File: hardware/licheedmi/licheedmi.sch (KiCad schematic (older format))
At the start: 70 parts, among them J1 Conn_01x09, J2 HDMI_A_PCB, J3 LicheePiNano_LCD, J4 HDMI_A, J5 USB_C_Receptacle_USB2.0, U1 TDA19988, U2 LicheeNano, U3 TS3DV20812, U4 SC6206B, U5 CH340C

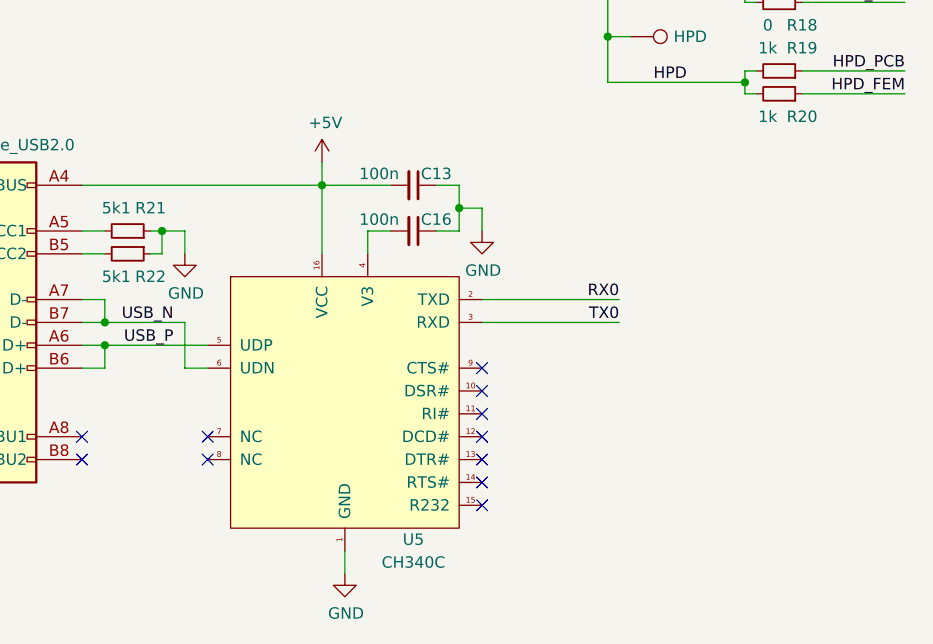
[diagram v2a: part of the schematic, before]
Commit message: sch, pcb: Add UART0 activity LEDs
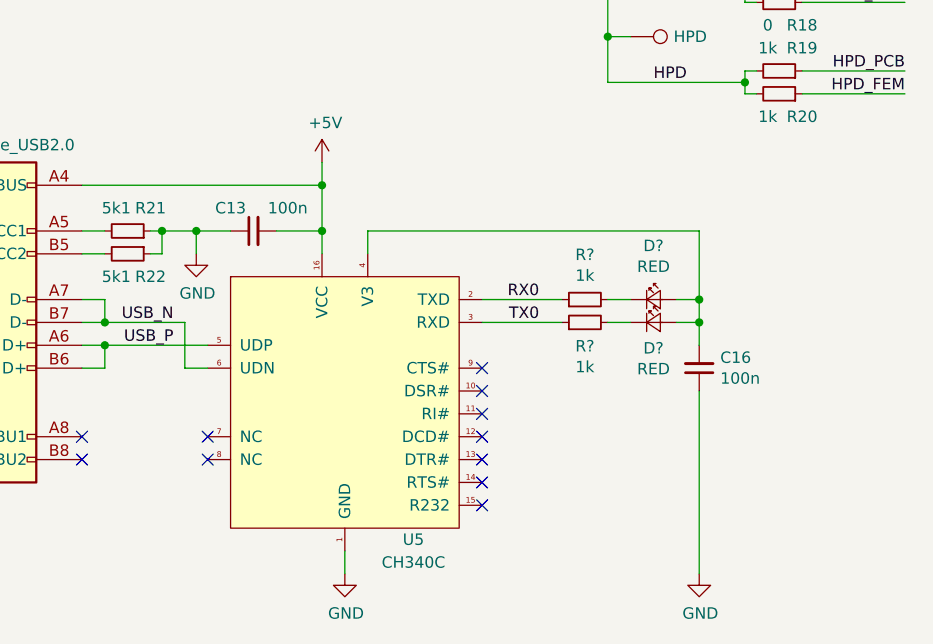
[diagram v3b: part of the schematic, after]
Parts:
- added D? (x2): RED, LED_SMD:LED_0603_1608Metric, symbol Device:LED_Small
- added R? (x2): 1k, Resistor_SMD:R_0603_1608Metric, symbol Device:R_Small
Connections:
- net RX0: now also R?.1
- net TX0: now also R?.1
- net at C16.2, U5.4 (V3): now also D?.2 (A), D?.2 (A)
- new net: D?.1 (K), R?.2 (x2)
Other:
- moved on the sheet: C13, C16
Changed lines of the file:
@@
 	7750 9250 7700 9250
 Wire Wire Line
-	7750 9150 7850 9150
-Wire Wire Line
-	7850 9150 7850 9250
+	7900 9150 7900 9250
 $Comp
 L power:GND #PWR040
 U 1 1 609CB49C
-P 7850 9250
-F 0 "#PWR040" H 7850 9000 50  0001 C CNN
-F 1 "GND" H 7855 9077 50  0000 C CNN
-F 2 "" H 7850 9250 50  0001 C CNN
-F 3 "" H 7850 9250 50  0001 C CNN
-	1    7850 9250
+P 7900 9250
+F 0 "#PWR040" H 7900 9000 50  0001 C CNN
+F 1 "GND" H 7905 9077 50  0000 C CNN
+F 2 "" H 7900 9250 50  0001 C CNN
+F 3 "" H 7900 9250 50  0001 C CNN
+	1    7900 9250
 	1    0    0    -1
 $EndComp
@@
 Connection ~ 7500 9550
 Wire Wire Line
-	8450 8950 8450 9250
+	8450 8950 8450 9150
 Wire Wire Line
 	8450 8950 7400 8950
-Wire Wire Line
-	8650 9250 8650 9150
-Wire Wire Line
-	8650 9150 8750 9150
-Wire Wire Line
-	8450 8950 8750 8950
 Connection ~ 8450 8950
-$Comp
-L Device:C_Small C16
-U 1 1 60B3D507
-P 8850 9150
-F 0 "C16" V 8800 9250 50  0000 C CNN
-F 1 "100n" V 8800 9000 50  0000 C CNN
-F 2 "Capacitor_SMD:C_0603_1608Metric" H 8850 9150 50  0001 C CNN
-F 3 "~" H 8850 9150 50  0001 C CNN
-F 4 "C1591" H 8850 9150 50  0001 C CNN "LCSC P/N"
-F 5 "CL10B104KB8NNNC" H 8850 9150 50  0001 C CNN "MFR P/N"
-	1    8850 9150
-	0    1    1    0
-$EndComp
-Wire Wire Line
-	8950 8950 9050 8950
-Wire Wire Line
-	9050 8950 9050 9050
-Wire Wire Line
-	9050 9150 8950 9150
-$Comp
-L power:GND #PWR039
-U 1 1 60C32C09
-P 9150 9150
-F 0 "#PWR039" H 9150 8900 50  0001 C CNN
-F 1 "GND" H 9155 8977 50  0000 C CNN
-F 2 "" H 9150 9150 50  0001 C CNN
-F 3 "" H 9150 9150 50  0001 C CNN
-	1    9150 9150
-	1    0    0    -1
-$EndComp
-Wire Wire Line
-	9150 9150 9150 9050
-Wire Wire Line
-	9150 9050 9050 9050
-Connection ~ 9050 9050
-Wire Wire Line
-	9050 9050 9050 9150
-$Comp
-L Device:C_Small C13
-U 1 1 60EA28B7
-P 8850 8950
-F 0 "C13" V 8800 9050 50  0000 C CNN
-F 1 "100n" V 8800 8800 50  0000 C CNN
-F 2 "Capacitor_SMD:C_0603_1608Metric" H 8850 8950 50  0001 C CNN
-F 3 "~" H 8850 8950 50  0001 C CNN
-F 4 "C1591" H 8850 8950 50  0001 C CNN "LCSC P/N"
-F 5 "CL10B104KB8NNNC" H 8850 8950 50  0001 C CNN "MFR P/N"
-	1    8850 8950
-	0    1    1    0
-$EndComp
 NoConn ~ 7400 10050
 NoConn ~ 7400 10150
@@
 NoConn ~ 9150 9850
 NoConn ~ 9150 9750
-Wire Wire Line
-	9150 9550 9750 9550
-Text Label 9750 9550 2    50   ~ 0
+Text Label 9400 9550 2    50   ~ 0
 TX0
-Wire Wire Line
-	9150 9450 9750 9450
-Text Label 9750 9450 2    50   ~ 0
+Text Label 9400 9450 2    50   ~ 0
 RX0
 $Comp
@@
 Text Label 7800 9550 2    50   ~ 0
 USB_N
+Wire Wire Line
+	9150 9450 9500 9450
+Wire Wire Line
+	9150 9550 9500 9550
+$Comp
+L Device:R_Small R?
+U 1 1 612667FD
+P 9600 9450
+F 0 "R?" V 9796 9450 50  0000 C CNN
+F 1 "1k" V 9705 9450 50  0000 C CNN
+F 2 "Resistor_SMD:R_0603_1608Metric" H 9600 9450 50  0001 C CNN
+F 3 "~" H 9600 9450 50  0001 C CNN
+F 4 "C380759" H 9600 9450 50  0001 C CNN "LCSC P/N"
+F 5 "SY0603JN1KP" H 9600 9450 50  0001 C CNN "MFR P/N"
+	1    9600 9450
+	0    -1   -1   0
+$EndComp
+Wire Wire Line
+	9800 9450 9700 9450
+$Comp
+L Device:R_Small R?
+U 1 1 612667F3
+P 9600 9550
+F 0 "R?" V 9496 9550 50  0000 C CNN
+F 1 "1k" V 9405 9550 50  0000 C CNN
+F 2 "Resistor_SMD:R_0603_1608Metric" H 9600 9550 50  0001 C CNN
+F 3 "~" H 9600 9550 50  0001 C CNN
+F 4 "C380759" H 9600 9550 50  0001 C CNN "LCSC P/N"
+F 5 "SY0603JN1KP" H 9600 9550 50  0001 C CNN "MFR P/N"
+	1    9600 9550
+	0    -1   -1   0
+$EndComp
+Wire Wire Line
+	8650 9250 8650 9150
+Wire Wire Line
+	9800 9550 9700 9550
+$Comp
+L Device:LED_Small D?
+U 1 1 61266805
+P 9900 9450
+F 0 "D?" H 9900 9685 50  0000 C CNN
+F 1 "RED" H 9900 9594 50  0000 C CNN
+F 2 "LED_SMD:LED_0603_1608Metric" V 9900 9450 50  0001 C CNN
+F 3 "~" V 9900 9450 50  0001 C CNN
+F 4 "C157741" H 9900 9450 50  0001 C CNN "LCSC P/N"
+F 5 "LTST-C193KRKT-5A" H 9900 9450 50  0001 C CNN "MFR P/N"
+	1    9900 9450
+	1    0    0    -1
+$EndComp
+$Comp
+L Device:LED_Small D?
+U 1 1 6126680D
+P 9900 9550
+F 0 "D?" H 9900 9437 50  0000 C CNN
+F 1 "RED" H 9900 9346 50  0000 C CNN
+F 2 "LED_SMD:LED_0603_1608Metric" V 9900 9550 50  0001 C CNN
+F 3 "~" V 9900 9550 50  0001 C CNN
+F 4 "C157741" H 9900 9550 50  0001 C CNN "LCSC P/N"
+F 5 "LTST-C193KRKT-5A" H 9900 9550 50  0001 C CNN "MFR P/N"
+	1    9900 9550
+	1    0    0    -1
+$EndComp
+Wire Wire Line
+	10000 9550 10100 9550
+Wire Wire Line
+	10100 9550 10100 9450
+Wire Wire Line
+	10000 9450 10100 9450
+Wire Wire Line
+	10100 9150 10100 9450
+Connection ~ 10100 9450
+Wire Wire Line
+	8650 9150 10100 9150
+$Comp
+L Device:C_Small C16
+U 1 1 60B3D507
+P 10100 9750
+F 0 "C16" H 10008 9704 50  0000 R CNN
+F 1 "100n" H 10008 9795 50  0000 R CNN
+F 2 "Capacitor_SMD:C_0603_1608Metric" H 10100 9750 50  0001 C CNN
+F 3 "~" H 10100 9750 50  0001 C CNN
+F 4 "C1591" H 10100 9750 50  0001 C CNN "LCSC P/N"
+F 5 "CL10B104KB8NNNC" H 10100 9750 50  0001 C CNN "MFR P/N"
+	1    10100 9750
+	-1   0    0    1
+$EndComp
+Wire Wire Line
+	8250 9150 8450 9150
+Connection ~ 8450 9150
+Wire Wire Line
+	8450 9150 8450 9250
+$Comp
+L Device:C_Small C13
+U 1 1 60EA28B7
+P 8150 9150
+F 0 "C13" V 8050 9250 50  0000 C CNN
+F 1 "100n" V 8050 9000 50  0000 C CNN
+F 2 "Capacitor_SMD:C_0603_1608Metric" H 8150 9150 50  0001 C CNN
+F 3 "~" H 8150 9150 50  0001 C CNN
+F 4 "C1591" H 8150 9150 50  0001 C CNN "LCSC P/N"
+F 5 "CL10B104KB8NNNC" H 8150 9150 50  0001 C CNN "MFR P/N"
+	1    8150 9150
+	0    -1   1    0
+$EndComp
+$Comp
+L power:GND #PWR?
+U 1 1 618D30BF
+P 10100 10650
+F 0 "#PWR?" H 10100 10400 50  0001 C CNN
+F 1 "GND" H 10105 10477 50  0000 C CNN
+F 2 "" H 10100 10650 50  0001 C CNN
+F 3 "" H 10100 10650 50  0001 C CNN
+	1    10100 10650
+	1    0    0    -1
+$EndComp
+Wire Wire Line
+	10100 10650 10100 9850
+Wire Wire Line
+	10100 9650 10100 9550
+Connection ~ 10100 9550
+Connection ~ 7900 9150
+Wire Wire Line
+	7900 9150 8050 9150
+Wire Wire Line
+	7750 9150 7900 9150
 $EndSCHEMATC

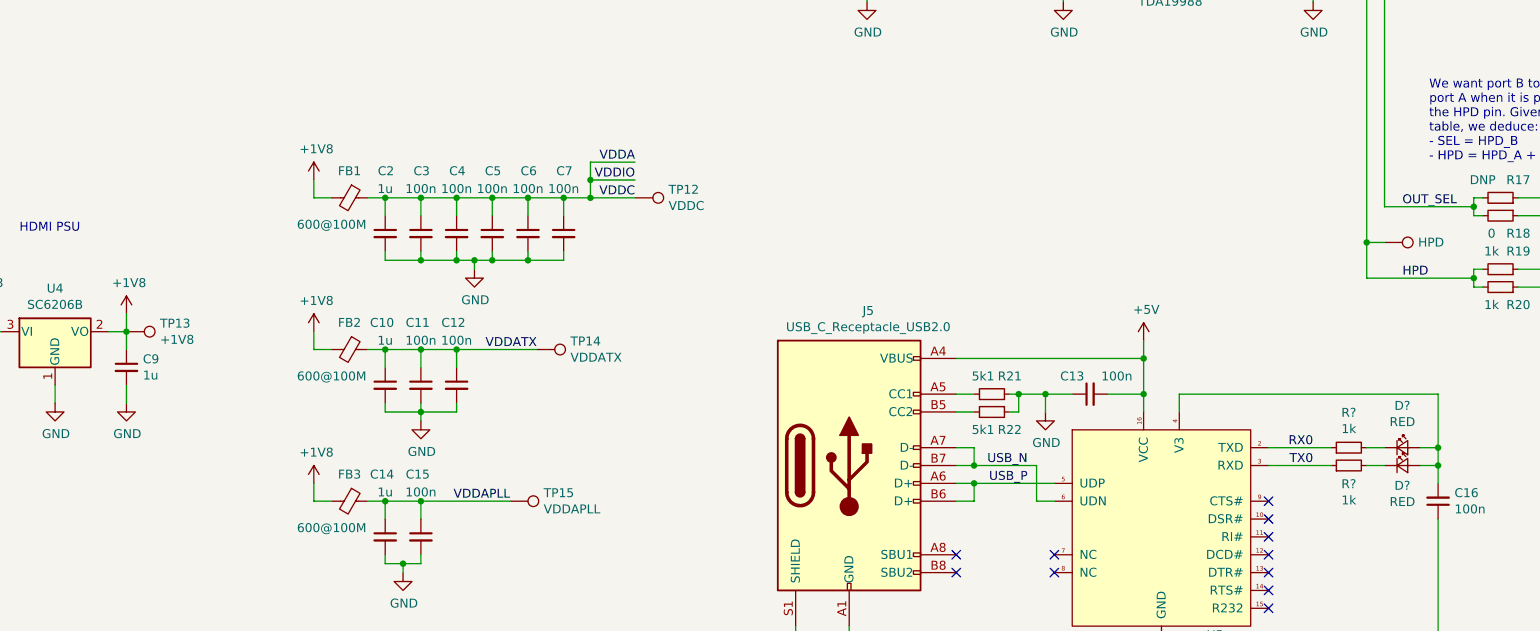
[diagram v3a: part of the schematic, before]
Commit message: sch: Fix real ERC issues
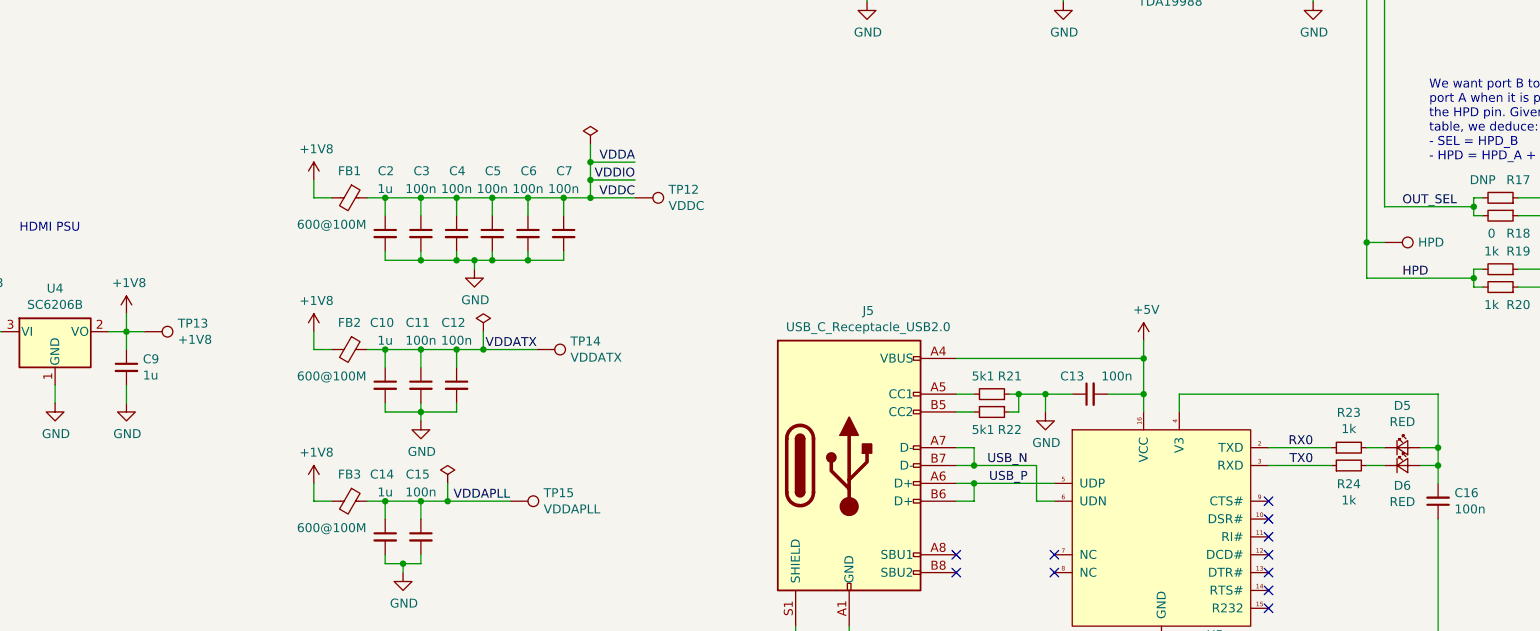
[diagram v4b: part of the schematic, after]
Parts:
- gave numbers to parts that had none: 4
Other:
- moved on the sheet: TP13
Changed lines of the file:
@@
 L Connector:TestPoint TP13
 U 1 1 615696EE
-P 2750 8800
-F 0 "TP13" V 2704 8988 50  0000 L CNN
-F 1 "+1V8" V 2795 8988 50  0000 L CNN
-F 2 "TestPoint:TestPoint_Pad_D1.0mm" H 2950 8800 50  0001 C CNN
-F 3 "~" H 2950 8800 50  0001 C CNN
-	1    2750 8800
+P 2850 8800
+F 0 "TP13" V 2804 8988 50  0000 L CNN
+F 1 "+1V8" V 2895 8988 50  0000 L CNN
+F 2 "TestPoint:TestPoint_Pad_D1.0mm" H 3050 8800 50  0001 C CNN
+F 3 "~" H 3050 8800 50  0001 C CNN
+	1    2850 8800
 	0    1    1    0
 $EndComp
@@
 	14900 4950 15000 4950
 Wire Wire Line
-	4600 8900 5050 8900
-Wire Wire Line
-	4400 9750 4900 9750
+	4600 8900 4750 8900
+Wire Wire Line
+	4400 9750 4550 9750
 Wire Wire Line
 	4400 9250 4600 9250
@@
 	9150 9550 9500 9550
 $Comp
-L Device:R_Small R?
+L Device:R_Small R23
 U 1 1 612667FD
 P 9600 9450
-F 0 "R?" V 9796 9450 50  0000 C CNN
+F 0 "R23" V 9796 9450 50  0000 C CNN
 F 1 "1k" V 9705 9450 50  0000 C CNN
 F 2 "Resistor_SMD:R_0603_1608Metric" H 9600 9450 50  0001 C CNN
@@
 	9800 9450 9700 9450
 $Comp
-L Device:R_Small R?
+L Device:R_Small R24
 U 1 1 612667F3
 P 9600 9550
-F 0 "R?" V 9496 9550 50  0000 C CNN
+F 0 "R24" V 9496 9550 50  0000 C CNN
 F 1 "1k" V 9405 9550 50  0000 C CNN
 F 2 "Resistor_SMD:R_0603_1608Metric" H 9600 9550 50  0001 C CNN
@@
 	9800 9550 9700 9550
 $Comp
-L Device:LED_Small D?
+L Device:LED_Small D5
 U 1 1 61266805
 P 9900 9450
-F 0 "D?" H 9900 9685 50  0000 C CNN
+F 0 "D5" H 9900 9685 50  0000 C CNN
 F 1 "RED" H 9900 9594 50  0000 C CNN
 F 2 "LED_SMD:LED_0603_1608Metric" V 9900 9450 50  0001 C CNN
@@
 $EndComp
 $Comp
-L Device:LED_Small D?
+L Device:LED_Small D6
 U 1 1 6126680D
 P 9900 9550
-F 0 "D?" H 9900 9437 50  0000 C CNN
+F 0 "D6" H 9900 9437 50  0000 C CNN
 F 1 "RED" H 9900 9346 50  0000 C CNN
 F 2 "LED_SMD:LED_0603_1608Metric" V 9900 9550 50  0001 C CNN
@@
 $EndComp
 $Comp
-L power:GND #PWR?
+L power:GND #PWR039
 U 1 1 618D30BF
 P 10100 10650
-F 0 "#PWR?" H 10100 10400 50  0001 C CNN
+F 0 "#PWR039" H 10100 10400 50  0001 C CNN
 F 1 "GND" H 10105 10477 50  0000 C CNN
 F 2 "" H 10100 10650 50  0001 C CNN
@@
 Wire Wire Line
 	7750 9150 7900 9150
+$Comp
+L power:PWR_FLAG #FLG0102
+U 1 1 61B75BCB
+P 5350 7750
+F 0 "#FLG0102" H 5350 7825 50  0001 C CNN
+F 1 "PWR_FLAG" H 5350 7923 50  0001 C CNN
+F 2 "" H 5350 7750 50  0001 C CNN
+F 3 "~" H 5350 7750 50  0001 C CNN
+	1    5350 7750
+	1    0    0    -1
+$EndComp
+$Comp
+L power:PWR_FLAG #FLG0103
+U 1 1 61B7666E
+P 4750 8800
+F 0 "#FLG0103" H 4750 8875 50  0001 C CNN
+F 1 "PWR_FLAG" H 4750 8973 50  0001 C CNN
+F 2 "" H 4750 8800 50  0001 C CNN
+F 3 "~" H 4750 8800 50  0001 C CNN
+	1    4750 8800
+	1    0    0    -1
+$EndComp
+$Comp
+L power:PWR_FLAG #FLG0104
+U 1 1 61B76D89
+P 4550 9650
+F 0 "#FLG0104" H 4550 9725 50  0001 C CNN
+F 1 "PWR_FLAG" H 4550 9823 50  0001 C CNN
+F 2 "" H 4550 9650 50  0001 C CNN
+F 3 "~" H 4550 9650 50  0001 C CNN
+	1    4550 9650
+	1    0    0    -1
+$EndComp
+Wire Wire Line
+	4550 9650 4550 9750
+Connection ~ 4550 9750
+Wire Wire Line
+	4550 9750 4900 9750
+Wire Wire Line
+	4750 8800 4750 8900
+Connection ~ 4750 8900
+Wire Wire Line
+	4750 8900 5050 8900
+Wire Wire Line
+	5350 7750 5350 7850
+Connection ~ 5350 7850
+Wire Wire Line
+	2750 8800 2850 8800
 $EndSCHEMATC

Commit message: sch: Add missing P/N for USB-C connector
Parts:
- J5: LCSC P/N (none) -> C165948; MFR P/N (none) -> TYPE-C-31-M-12
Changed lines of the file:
@@
 F 2 "hdmizness:USB_C_Receptacle_Palconn_UTC16-G" H 6950 9550 50  0001 C CNN
 F 3 "https://www.usb.org/sites/default/files/documents/usb_type-c.zip" H 6950 9550 50  0001 C CNN
+F 4 "C165948" H 6800 9550 50  0001 C CNN "LCSC P/N"
+F 5 "TYPE-C-31-M-12" H 6800 9550 50  0001 C CNN "MFR P/N"
 	1    6800 9550
 	1    0    0    -1

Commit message: Add FPC connector 3D model
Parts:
- J3: footprint Connector_FFC-FPC:Hirose_FH12-40S-0.5SH_1x40-1MP_P0.50mm_Horizontal -> hdmizness:Hirose_FH12-40S-0.5SH_1x40-1MP_P0.50mm_Horizontal
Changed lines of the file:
@@
 F 0 "J3" H 5543 6475 50  0000 C CNN
 F 1 "LicheePiNano_LCD" H 5543 6384 50  0000 C CNN
-F 2 "Connector_FFC-FPC:Hirose_FH12-40S-0.5SH_1x40-1MP_P0.50mm_Horizontal" H 5350 4350 50  0001 C CNN
+F 2 "hdmizness:Hirose_FH12-40S-0.5SH_1x40-1MP_P0.50mm_Horizontal" H 5350 4350 50  0001 C CNN
 F 3 "${KIPRJMOD}/../../documentation/lichee_nano_8.16_schematic.pdf" H 5350 4350 50  0001 C CNN
 F 4 "C202114" H 5400 4350 50  0001 C CNN "LCSC P/N"
